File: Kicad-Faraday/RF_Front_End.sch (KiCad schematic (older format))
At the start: 18 parts, among them U4 CC1190, U5 SF2049E

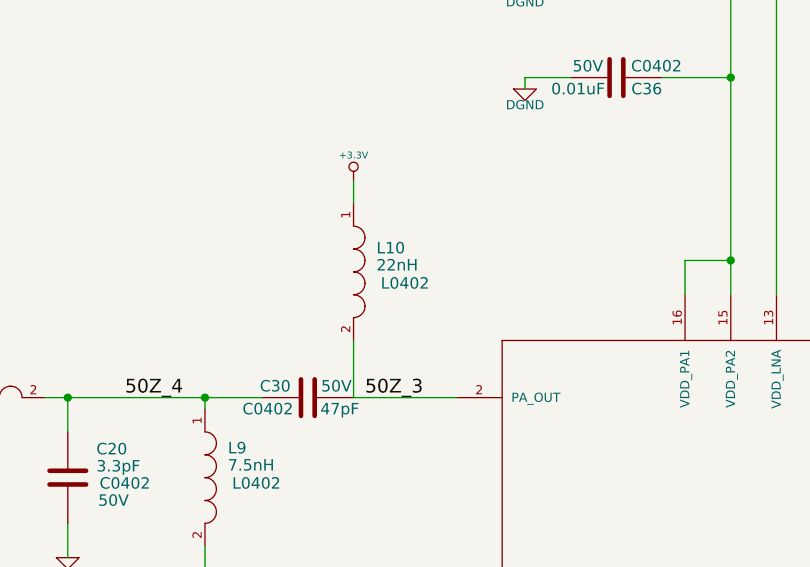
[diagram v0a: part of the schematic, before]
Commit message: Updated several items from the Rev B to C updates including microphone RC filter and CC1190 inductor footprints.
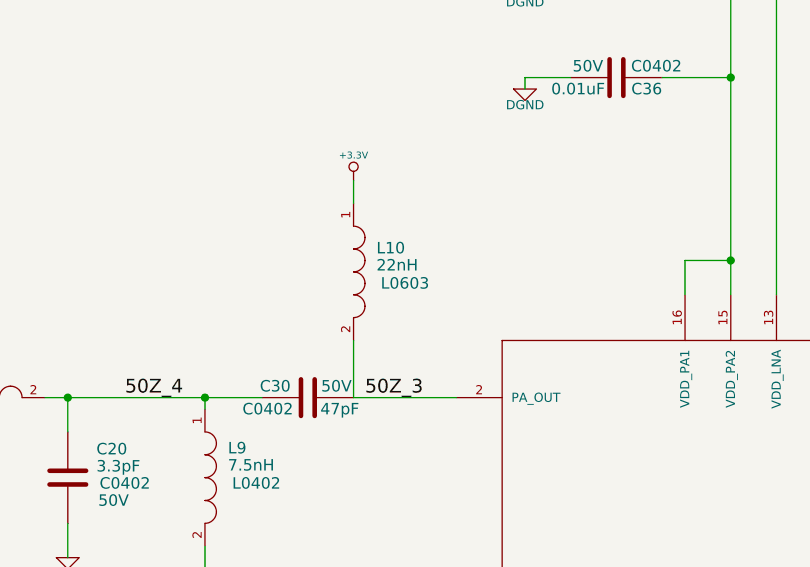
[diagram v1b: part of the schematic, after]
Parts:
- L10: footprint L0402 -> L0603
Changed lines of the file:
@@
 Sheet 7 11
 Title "Faraday Wireless Node"
-Date "8 aug 2016"
+Date "18 oct 2016"
 Rev "C"
 Comp "FaradayRF"
@@
 F 0 "L10" H 7150 5025 50  0000 L BNN
 F 1 "22nH" H 7150 4950 50  0000 L BNN
-F 2 "L0402" H 7275 4900 50  0000 C CNN
+F 2 "L0603" H 7275 4900 50  0000 C CNN
 F 3 "" H 7050 4950 60  0000 C CNN
 	1    7050 4950
